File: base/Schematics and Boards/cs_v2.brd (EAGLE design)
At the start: 35.6 x 33.8 mm, 81 parts, among them J101 J-JTAG-CORTEX-NEEDLE6, J102 J-MICROSD-DM3AT-SF-PEJM5, J301 HIROSE-DF40_44-PIN_CONNECTORS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, J302 HIROSE-DF40_30-PIN_CONNECTORS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, Q201 FK3303010L, Q202 FK3303010L, Q203 FK3303010L, Q204 DMG3415UFY4Q-7, U101 ATSAMD51, U201 COULOMB-MAX17262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

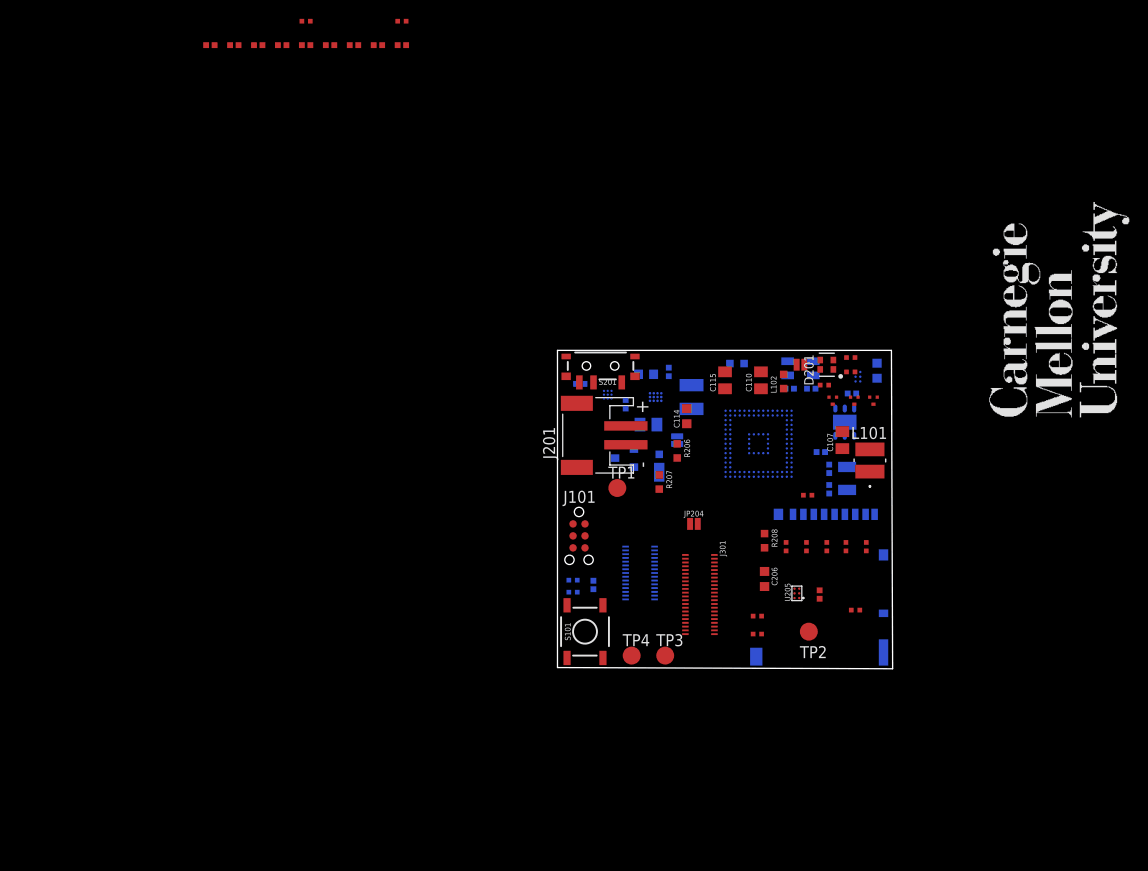
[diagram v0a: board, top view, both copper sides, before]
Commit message: Move CC after power selection. Add SPI flash over SD. Swap PowSel diode
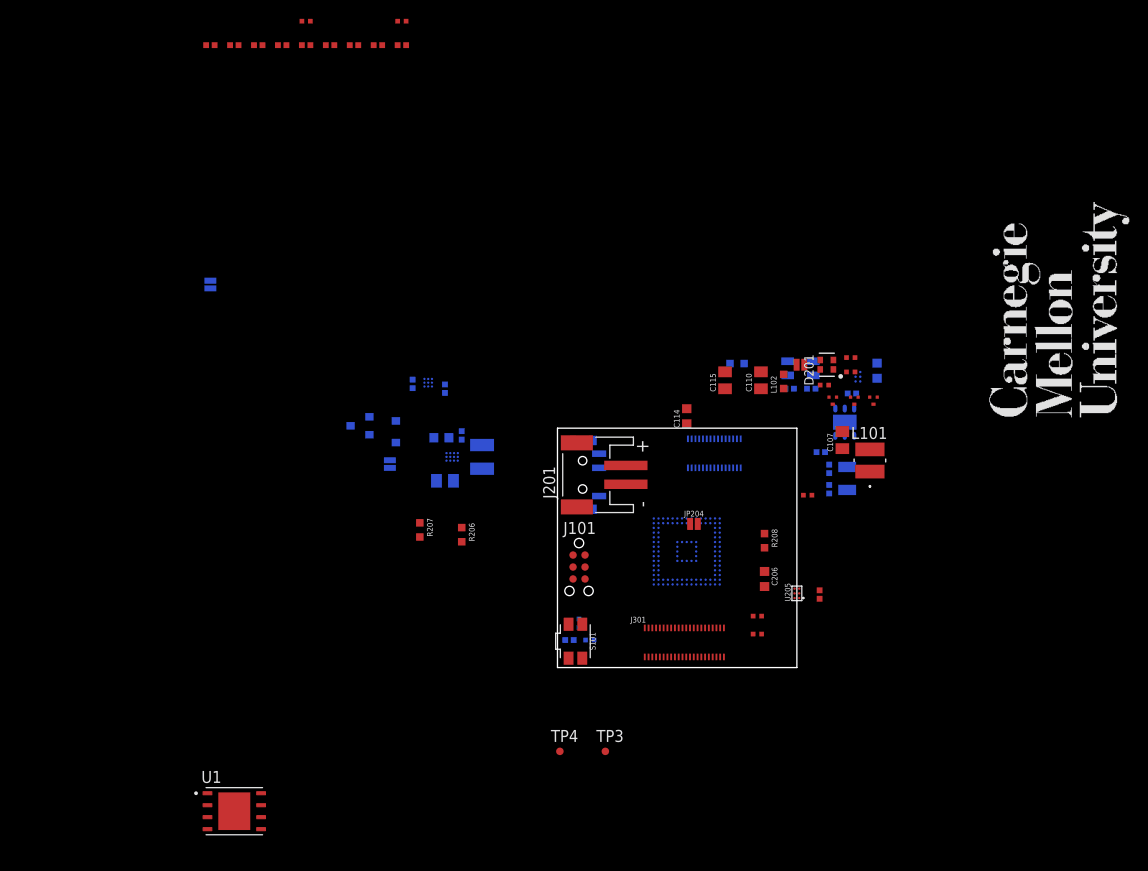
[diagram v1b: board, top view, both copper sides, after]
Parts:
- removed J102: J-MICROSD-DM3AT-SF-PEJM5, Connectors:MICRO-SD
- removed JP201, JP203: JUMPER-SMT_2_NC_PASTE_NO-SILK, Connectors:SMT-JUMPER_2_NC_PASTE_NO-SILK
- removed R105, R107, R108, R109: 100K, Resistors:R0402
- removed R110: 10K, Resistors:R0402
- removed R111: 510k, Resistors:R0402
- removed TP1, TP2: PTR1TP19R, TestPoints:TP19R
- added JP_PROC, JP_VDBG: JUMPER-SMT_2_NC_PASTE_NO-SILK, Connectors:SMT-JUMPER_2_NC_PASTE_NO-SILK
- added U1: AT25SF641-MHB-T, Storage:8-UDFN
- R204: value 100k -> 10M
- S101: value MOMENTARY-SWITCH-SPST-SMD-5.2-REDUNDANT -> SW_EVQ-P7L01P_SPST_RA; device Switches:TACTILE_SWITCH_SMD_5.2MM -> Switches:SW_EVQ-P7L01P
- TP3, TP4: value PTR1TP19R -> TPTP08R; device TestPoints:TP19R -> TestPoints:TP08R
- U202: value PD3S140-7 -> CUS520H3F; device Diodes:POWERDI323 -> Diodes:CUS520H3F
- moved Q204 28.3 mm to (-21.0, 25.7)
- moved U202 28.1 mm to (-17.1, 25.0), turned to 270 degrees
- moved R207 25.9 mm to (-14.6, 14.6)
- moved R206 24.5 mm to (-10.2, 14.1)
- moved L201 23.1 mm to (-8.00, 22.4)
- moved C204 23.0 mm to (-10.2, 24.6)
- moved C202 22.7 mm to (-12.3, 24.4)
- moved U203 22.5 mm to (-11.2, 22.4)
- moved C205 22.4 mm to (-11.9, 19.8)
- moved C203 19.2 mm to (-11.9, 29.6)
- moved U201 19.1 mm to (-13.7, 30.2)
- moved C201 17.8 mm to (-15.4, 30.1), turned to 270 degrees
- moved J302 14.9 mm to (16.6, 22.7), turned to 180 degrees
- moved U101 13.7 mm to (13.7, 12.3)
- moved TP4 12.7 mm to (0.25, -8.89)
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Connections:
- net +3V3_SD_SENSE renamed +3V3_STOR_SENSE
- removed net +3V3_SD: C208.1, J102.4, R105.2, R107.2, R108.2, R109.2, R110.2, R111.1, TP2.TP, U205.A1, U205.B1
- removed net +3V7_BATT_IN: C201.1, S201.3, U201.A1, U201.A2
- removed net BATT+: J201.1, S201.2
- removed net BATT_ALERT: U201.B2
- removed net EN_SD: U101.PB01, U205.C2
- removed net N$8: S201.1
- removed net SD_CD: J102.SWA, R111.2, U101.PD20
- removed net SD_CLK: J102.5, U101.PA21
- removed net SD_CMD: J102.3, R110.1, U101.PA20
- removed net SD_D0: J102.7, R109.1, U101.PB18
- removed net SD_D1: J102.8, R108.1, U101.PB19
- removed net SD_D2: J102.1, R107.1, U101.PB20
- removed net SD_D3: J102.2, R105.1, U101.PB21
- new net +3V3_STOR: C208.1, U1.8, U205.A1, U205.B1
- new net CC_IN: C201.1, S201.1, U201.A1, U201.A2
- new net EN_STOR: U101.PC06, U205.C2
- new net STOR_HOLD: U1.7, U101.PB07
- new net STOR_SPI5_MISO: U1.2, U101.PB03
- new net STOR_SPI5_MOSI: U1.5, U101.PB00
- new net STOR_SPI5_NCS: U1.1, U101.PB02
- new net STOR_SPI5_SCK: U1.6, U101.PB01
- new net STOR_WP: U1.3, U101.PB06
- new net VDD_SW: Q204.2, S201.2, U202.N
- net +3V3_PROC: now also JP_PROC.1; no longer JP203.1
- net +3V7_BATT: now also J201.1; no longer TP1.TP, U201.B3
- net EN_TEMP: now also U101.PC07; no longer U101.PB00
- net GND: now also S101.2_1, S101.2_2, U1.4, U1.9; no longer J102.6, J102.P1, J102.P2, J102.P3, J102.P4, J102.SWB, S101.3, S101.4
- net N$19: now also JP_PROC.2; no longer JP203.2
- net N$5: now also S101.1_1, S101.1_2; no longer S101.1, S101.2
- net VDD_DBG: now also JP_VDBG.2; no longer JP201.2
- net VDD_DBG_JMP: now also JP_VDBG.1, U202.P; no longer JP201.1, U202.1
- net VREG_IN: now also U201.B3; no longer Q204.2, U202.2
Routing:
- added copper zone on layer 15, net +3V3_PROC
- added copper zone on layer 15, net +3V3_STOR
- removed copper zone on layer 14, net +3V3_PROC
- removed copper zone on layer 14, net +3V3_SD
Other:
- board size 35.6 x 33.8 mm -> 25.4 x 25.4 mm

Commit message: Minor sh changes; placed compressed power subsys, gitignore temp files
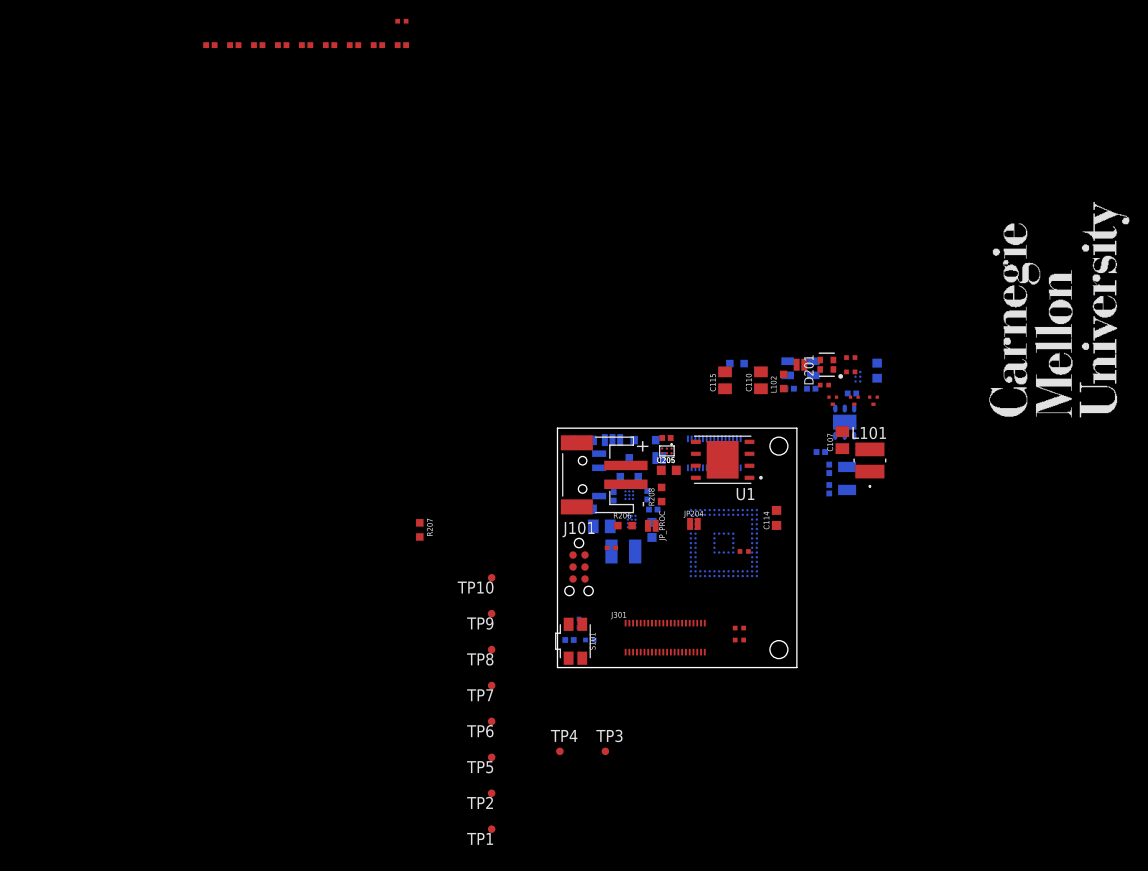
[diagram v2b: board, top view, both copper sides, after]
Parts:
- added JP1: JUMPER-SMT_3_1-NC_PASTE_NO-SILK, SparkFun-Jumpers:SMT-JUMPER_3_1-NC_PASTE_NO-SILK
- added TP1, TP10, TP2, TP5, TP6, TP7, TP8, TP9: TPTP08R, TestPoints:TP08R
- moved R112 64.6 mm to (5.71, 12.7)
- moved U1 63.8 mm to (17.5, 22.0), turned to 180 degrees
- moved JP_PROC 53.4 mm to (10.0, 15.0), flipped to the top, turned to 180 degrees
- moved Q204 28.9 mm to (7.62, 21.2), turned to 0 degrees
- moved JP_VDBG 28.6 mm to (10.8, 22.2), turned to 180 degrees
- moved U202 26.4 mm to (9.27, 24.1), turned to 180 degrees
- moved C201 24.4 mm to (5.97, 18.2)
- moved U201 24.4 mm to (7.62, 18.3)
- moved C202 24.4 mm to (10.0, 14.6), turned to 270 degrees
- moved C203 24.3 mm to (9.53, 18.3)
- moved C208 23.2 mm to (11.6, 24.4), turned to 180 degrees
- moved C204 21.8 mm to (10.2, 16.8), turned to 180 degrees
- moved U205 20.5 mm to (11.6, 23.0), turned to 270 degrees
- moved U203 20.2 mm to (7.87, 15.5), turned to 90 degrees
- moved L201 18.0 mm to (6.99, 12.3), turned to 0 degrees
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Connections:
- net N$18 renamed +3V3_DTR_SENSE
- net N$19 renamed +3V3_PROC_SENSE
- new net VDD_SW_IN: JP1.2, S201.2
- net +3V3_DTR: now also TP6.TP
- net +3V3_PROC: now also TP5.TP
- net +3V3_STOR: now also TP8.TP
- net +3V3_TEMP: now also TP7.TP
- net +3V7_BATT: now also JP1.1
- net CC_IN: now also S201.3; no longer S201.1
- net DTR_MASTER_I2C_SCL: now also TP10.TP
- net DTR_MASTER_I2C_SDA: now also TP9.TP
- net N$1: now also TP1.TP
- net VDD_SW: now also JP1.3; no longer S201.2
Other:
- board text added: "Design needs screws, but must be v small #0 screws have 60 mil diameter. M1.6 may work (70 mil clearance) M0.6 screws also exist Added two place(hole)ders at 70 mils"

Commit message: Board placement for 1in x 1in. Unrouted
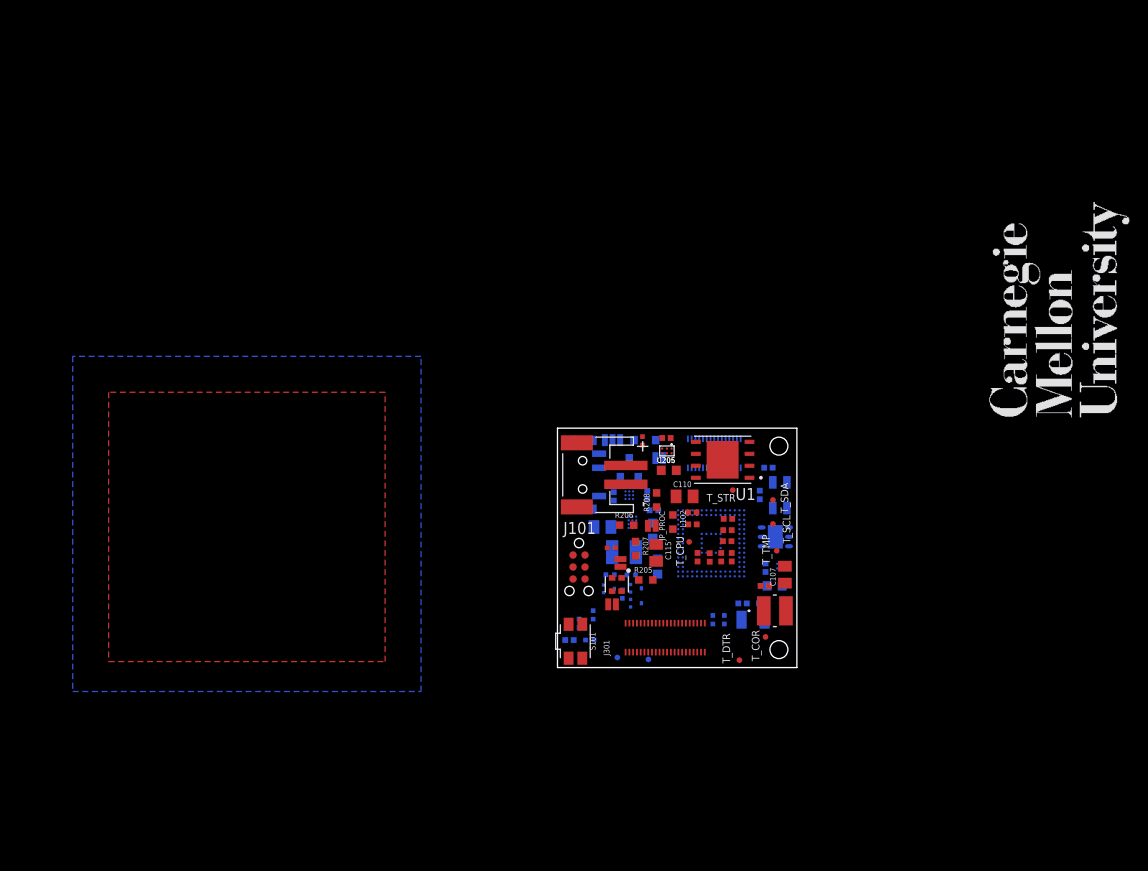
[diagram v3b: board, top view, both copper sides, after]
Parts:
- removed TP1, TP10, TP2, TP3, TP4, TP5, TP6, TP7, TP8, TP9: TPTP08R, TestPoints:TP08R
- added T_COR, T_CPU, T_DTR, T_RX, T_SCL, T_SDA, T_STR, T_TMP, T_TX: TPTP06R, TestPoints:TP06R
- moved C113 71.6 mm to (18.0, 14.6), turned to 180 degrees
- moved C108 71.2 mm to (14.3, 16.5)
- moved C105 70.4 mm to (14.3, 15.2)
- moved C109 69.1 mm to (18.5, 11.7), turned to 270 degrees
- moved C111 69.0 mm to (18.0, 13.4), turned to 180 degrees
- moved C112 69.0 mm to (18.1, 15.8), turned to 180 degrees
- moved C106 66.9 mm to (17.4, 11.7), turned to 270 degrees
- moved C104 64.8 mm to (16.2, 11.7), turned to 270 degrees
- moved C102 62.7 mm to (14.9, 11.7), turned to 270 degrees
- moved R204 51.3 mm to (9.02, 24.1), turned to 90 degrees
- moved R201 34.4 mm to (5.59, 9.86), flipped to the bottom
- moved Q201 34.2 mm to (5.46, 8.36), flipped to the bottom, turned to 90 degrees
- moved JP202 32.3 mm to (5.79, 6.71), turned to 0 degrees
- moved D201 32.2 mm to (6.30, 8.81), turned to 270 degrees
- moved R202 31.7 mm to (7.82, 9.83), flipped to the bottom, turned to 180 degrees
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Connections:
- net N$2 renamed VSW
- net N$3 renamed VDDANA
- removed net N$1: C103.1, C107.1, L101.2, TP1.TP, U101.VDDCORE
- new net VDDCORE: C103.1, C107.1, L101.2, T_COR.TP, U101.VDDCORE
- net +3V3_DTR: now also T_DTR.TP; no longer TP6.TP
- net +3V3_PROC: now also T_CPU.TP; no longer TP5.TP
- net +3V3_STOR: now also T_STR.TP; no longer TP8.TP
- net +3V3_TEMP: now also T_TMP.TP; no longer TP7.TP
- net DBG_SERIAL_RX: now also T_RX.TP; no longer TP3.TP
- net DBG_SERIAL_TX: now also T_TX.TP; no longer TP4.TP
- net DTR_MASTER_I2C_SCL: now also T_SCL.TP; no longer TP10.TP
- net DTR_MASTER_I2C_SDA: now also T_SDA.TP; no longer TP9.TP
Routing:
- added copper zone on layer 1, net GND
- added copper zone on layer 16, net GND
